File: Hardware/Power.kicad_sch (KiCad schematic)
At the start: 37 parts, among them U11 AP2112K-3.3, U5 AP2112K-3.3, U6 REC15E-2405SZ, U7 Ag9905M

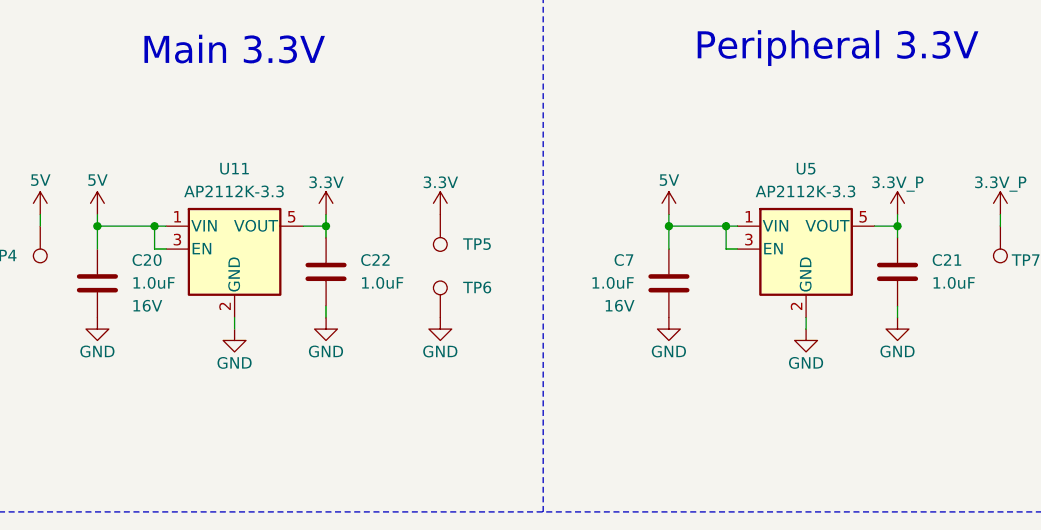
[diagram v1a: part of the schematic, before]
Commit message: Updates for v1.0 PCB
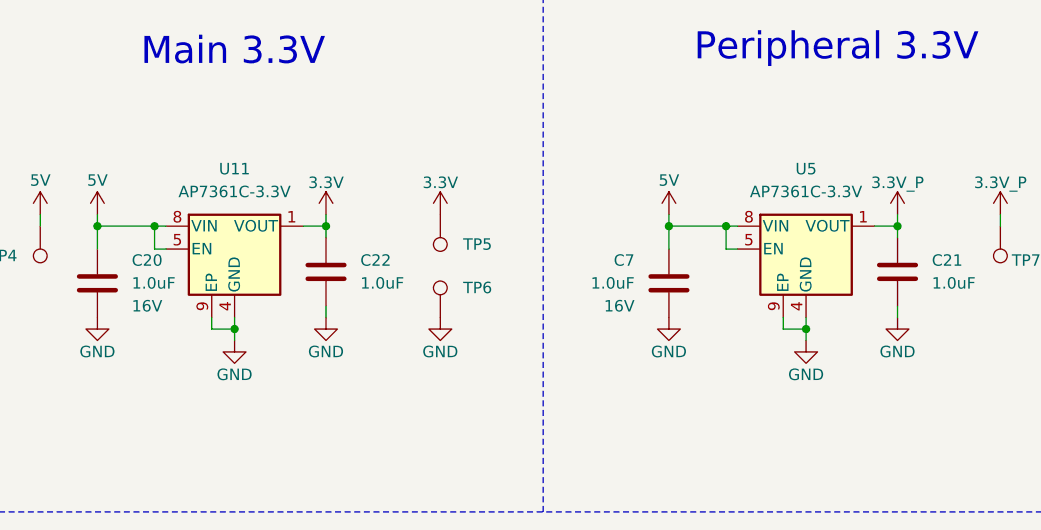
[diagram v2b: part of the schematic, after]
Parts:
- removed U11, U5: AP2112K-3.3, SparkFun-Semiconductor-Standard:SOT23-5, symbol SparkFun-Regulator:AP2112K-3.3
- added U11, U5: AP7361C-3.3V, SparkFun-Semiconductor-Standard:UDFN-8, symbol SparkFun-Regulator:AP7361C-3.3V
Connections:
- net 3.3V: now also U11.1 (VOUT)
- net 3.3V_P: now also U5.1 (VOUT)
- net 5V: now also U11.5 (EN), U11.8 (VIN), U5.5 (EN), U5.8 (VIN)
- net GND: now also U11.4 (GND), U11.9 (EP), U5.4 (GND), U5.9 (EP)
- new net: U11.2 (NC), U11.3 (NC), U11.6 (NC), U11.7 (NC)
- new net: U5.2 (NC), U5.3 (NC), U5.6 (NC), U5.7 (NC)
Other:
- title: (none) -> Power

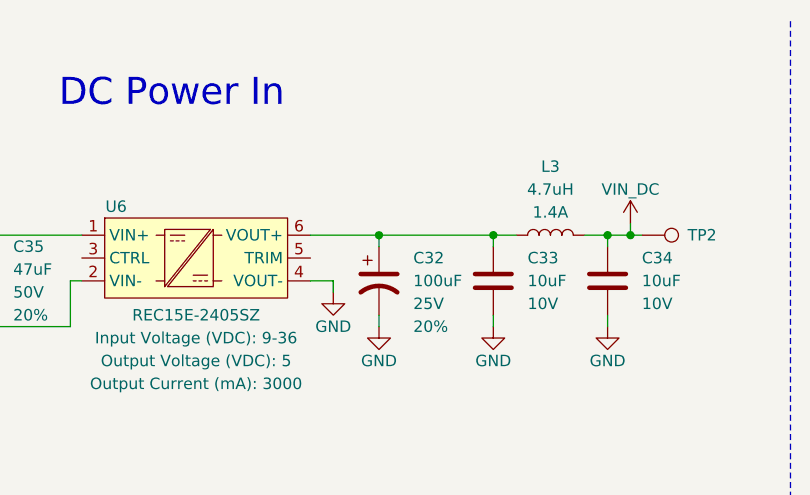
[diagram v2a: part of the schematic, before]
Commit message: Add mounting holes for SiT5811 / Rakon oscillator
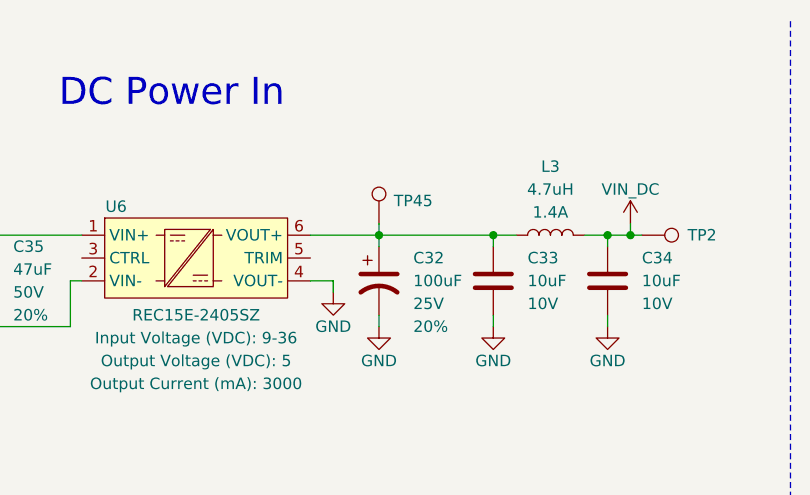
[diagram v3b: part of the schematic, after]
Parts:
- added TP45: PTH, SparkFun-Connector:1x01, symbol SparkFun-Connector:TestPoint_PTH
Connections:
- net at C32.1, C33.1, L3.1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: now also TP45.1
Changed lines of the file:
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@@
 	(wire
 		(pts
+			(xy 91.44 35.56) (xy 91.44 36.83)
+		)
+		(stroke
+			(width 0)
+			(type default)
+		)
+	)
+	(wire
+		(pts
 			(xy 91.44 36.83) (xy 104.14 36.83)
 		)
@@
 					(unit 1)
 				)
+			)
+		)
+	)
+	(symbol
+		(lib_id "SparkFun-Connector:TestPoint_PTH")
+		(at 91.44 35.56 0)
+		(mirror y)
+		(unit 1)
+		(exclude_from_sim no)
+		(in_bom yes)
+		(on_board yes)
+		(dnp no)
+		(property "Reference" "TP45"
+			(at 95.25 33.02 0)
+			(do_not_autoplace yes)
+			(effects
+				(font
+					(size 1.27 1.27)
+				)
+			)
+		)
+		(property "Value" "PTH"
+			(at 91.44 39.37 0)
+			(effects
+				(font
+					(size 1.27 1.27)
+				)
+				(hide yes)
+			)
+		)
+		(property "Footprint" "SparkFun-Connector:1x01"
+			(at 92.71 41.91 0)
+			(effects
+				(font
+					(size 1.27 1.27)
+				)
+				(hide yes)
+			)
+		)
+		(property "Datasheet" "~"
+			(at 91.44 43.18 0)
+			(effects
+				(font
+					(size 1.27 1.27)
+				)
+				(hide yes)
+			)
+		)
+		(property "Description" "Test Point"
+			(at 91.44 35.56 0)
+			(effects
+				(font
+					(size 1.27 1.27)
+				)
+				(hide yes)
+			)
+		)
+		(pin "1"
+		)
+		(instances
+			(project "SparkFun_RTK_mosaic-T"
+				(path "/e3dd3ae4-244d-4cba-9cca-5d2abf83f29a/476b4701-5340-4853-910a-2af933cad777"
+					(reference "TP45")
+					(unit 1)
+				)

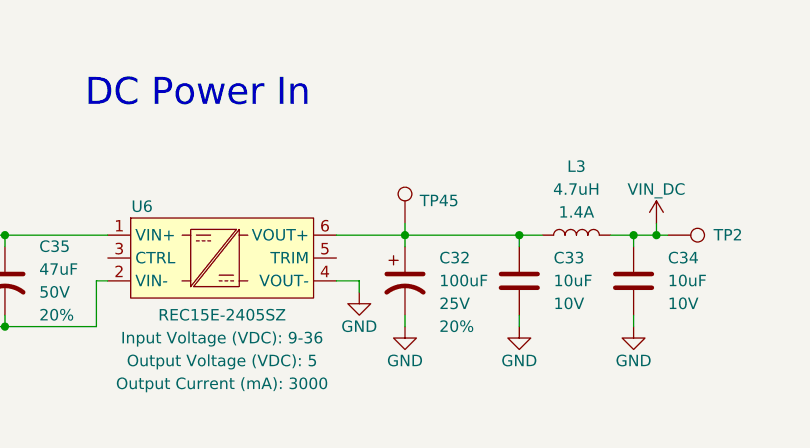
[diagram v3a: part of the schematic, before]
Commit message: Change KiCad file name to SparkPNT_GPSDO
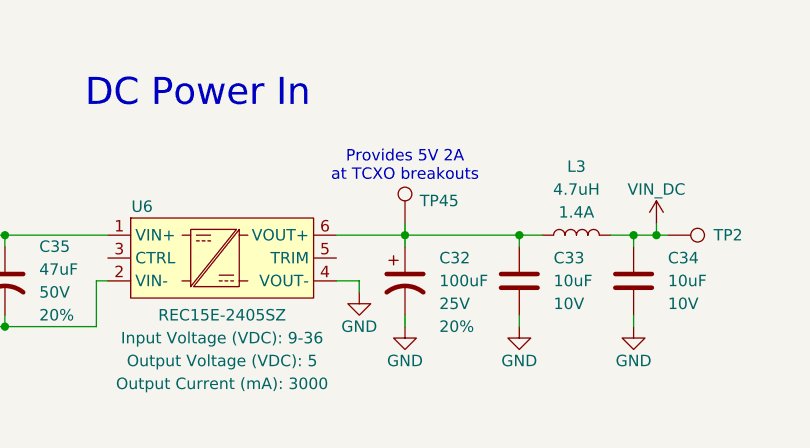
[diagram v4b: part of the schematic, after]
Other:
- note added: "Provides 5V 2A at TCXO breakouts"
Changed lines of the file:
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@@
+		)
+	)
+	(text "Provides 5V 2A\nat TCXO breakouts"
+		(exclude_from_sim no)
+		(at 91.44 29.21 0)
+		(effects
+			(font
+				(size 1.27 1.27)
+			)
 		)
 	)

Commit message: Final tweaks
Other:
- note added: "Provides 5V 2A for optional TCXO"
- note removed: "Provides 5V 2A at TCXO breakouts"
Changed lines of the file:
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@@
 		)
 	)
-	(text "Provides 5V 2A\nat TCXO breakouts"
+	(text "Provides 5V 2A\nfor optional TCXO"
 		(exclude_from_sim no)
 		(at 91.44 29.21 0)
